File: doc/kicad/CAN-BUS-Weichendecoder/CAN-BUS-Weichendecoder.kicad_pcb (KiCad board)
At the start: 2 copper layers, 158.8 x 124.5 mm, 53 parts, among them J1 250-1404, J1001 Conn_01x02_Female, J1003 Conn_01x07_Female, J11 250-1406, J12 Wago 250-1406, J13 Wago 250-1406, J14 Wago 250-1406, J15 Wago 250-1406, J2 250-1404, J22 J22, J23 J22, J3 250-1404, J31 12V DC, J4 250-1404, J41 2604-1102, J5 250-1404, U1 Arduino_Nano, U10 TSR_1-2450, U1001 6N136, U2 ULN2803A, U3 ULN2803A, U4 PCF8574, U5 PCF8574, U6 PCF8574, U7 ULN2803A, U8 ULN2803A, U9 ULN2803A

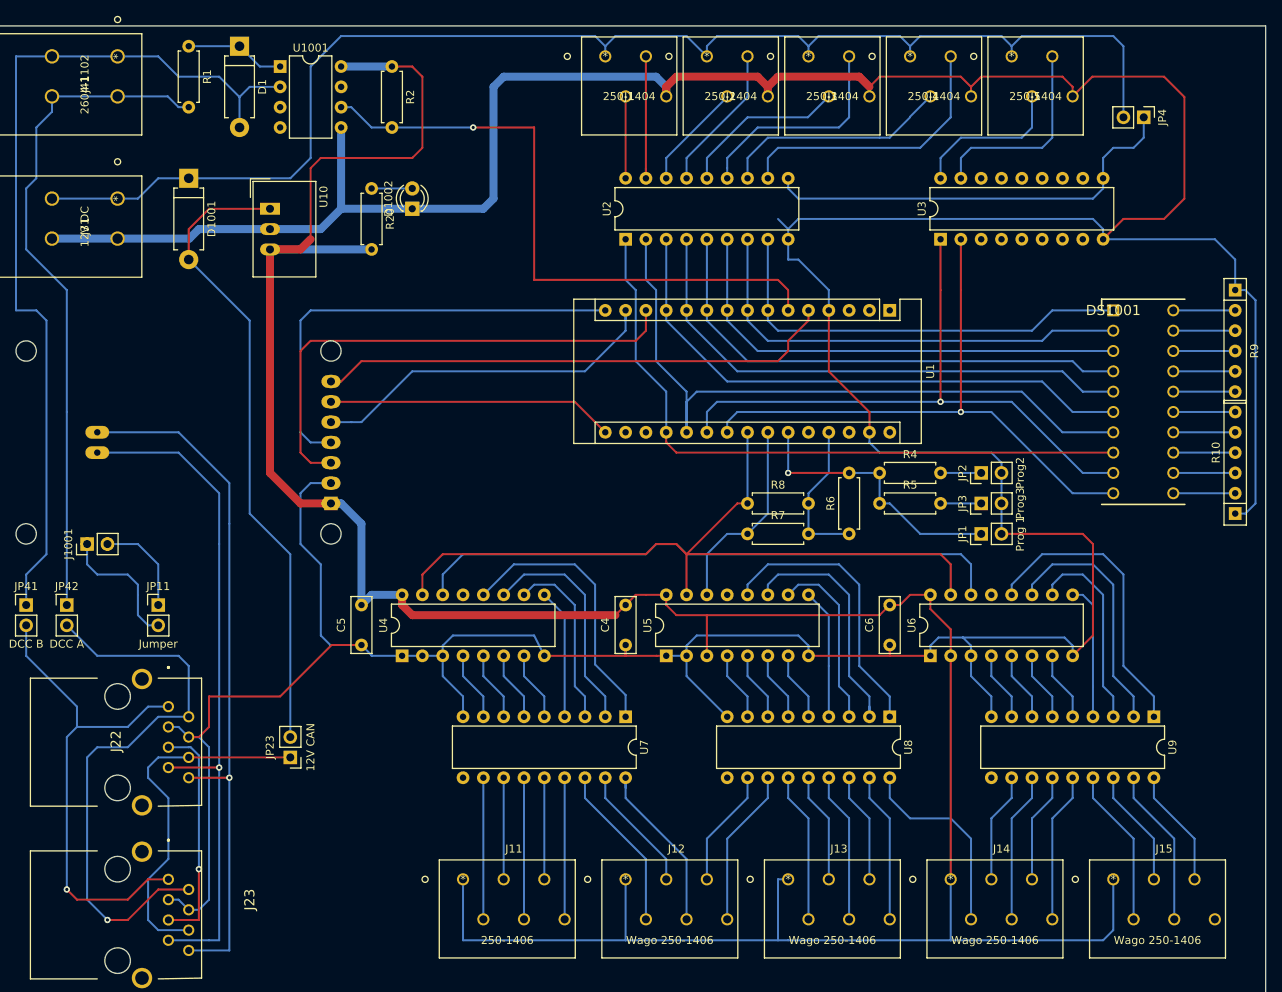
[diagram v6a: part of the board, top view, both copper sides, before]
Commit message: +5 analog zu GND verlegt
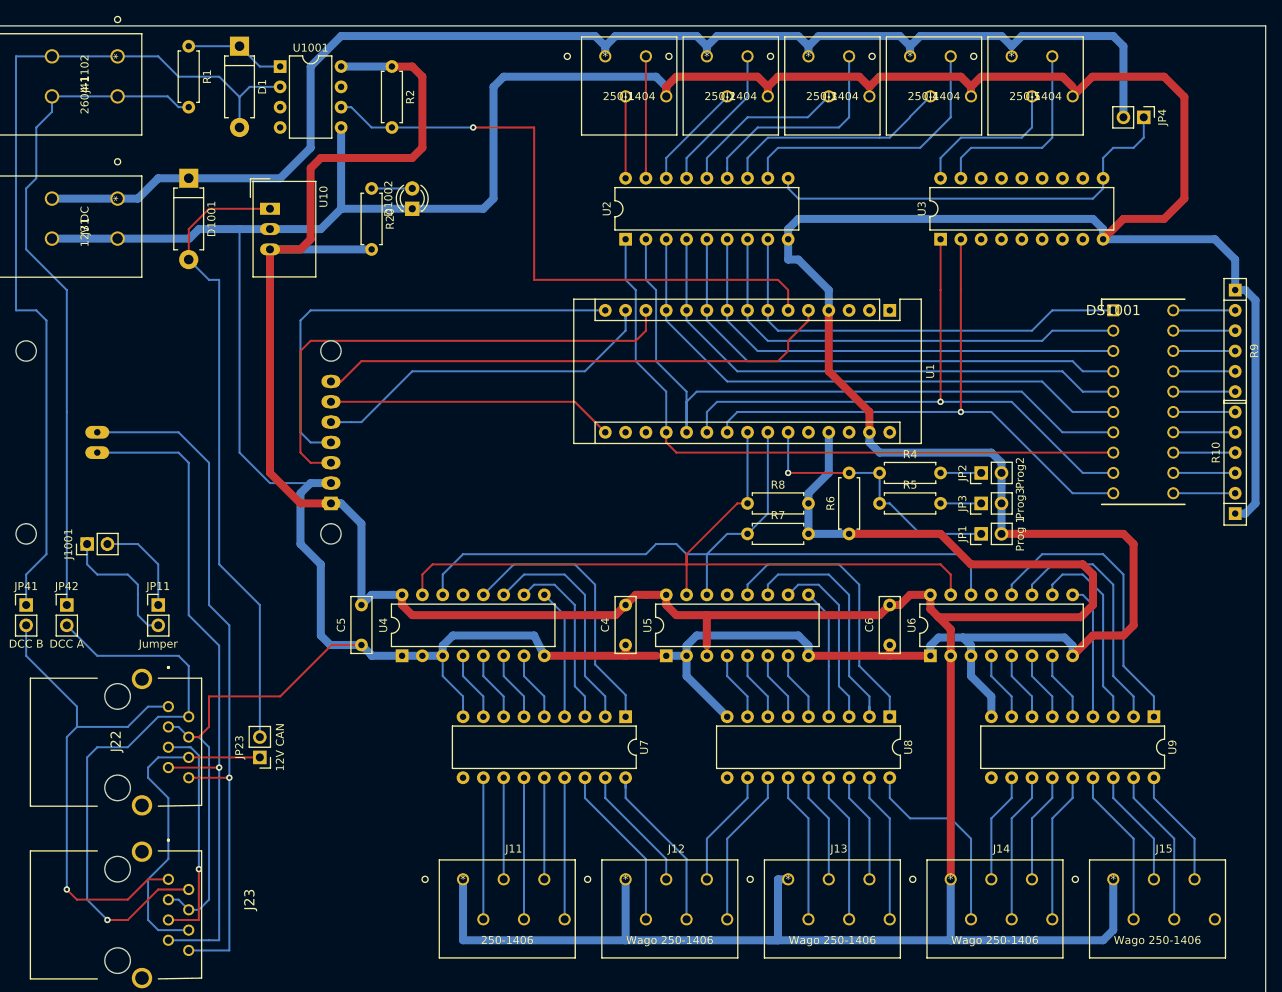
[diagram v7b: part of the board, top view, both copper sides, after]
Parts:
- moved JP23 3.81 mm to (86.4, 143.5)
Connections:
- Shield1001 pad 1: (no net) -> +5V
- Shield1001 pad 2: (no net) -> GND
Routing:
- net +5V: track 372.1 -> 429.7 mm
- net GND: track 611.2 -> 657.2 mm
- net Net-(J22-Pad6): track 45.1 -> 41.3 mm
- net Net-(R8-Pad1): track 99.2 -> 97.7 mm
- net +12V: track 170.6 -> 169.3 mm
- net Net-(D1001-Pad2): track 80.0 -> 79.1 mm

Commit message: verbessert
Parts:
- removed J1001: Conn_01x02_Female, Pin_Headers:Pin_Header_Straight_1x02_Pitch2.54mm
- removed J1003: Conn_01x07_Female, Pin_Headers:Pin_Header_Straight_1x07_Pitch2.54mm
- added H1: MountingHole, Mounting_Holes:MountingHole_3.2mm_M3, F.Cu at (207.0, 57.1)
- added H2: MountingHole, Mounting_Holes:MountingHole_3.2mm_M3, F.Cu at (205.7, 143.5)
- added H3: MountingHole, Mounting_Holes:MountingHole_3.2mm_M3, F.Cu at (114.3, 105.4)
- added H4: MountingHole, Mounting_Holes:MountingHole_3.2mm_M3, F.Cu at (101.6, 163.8)
- moved D1 10.2 mm to (94.0, 54.6)
- moved U10 10.2 mm to (97.8, 74.9)
- moved D1001 10.2 mm to (87.6, 71.1)
- moved D1002 10.2 mm to (115.6, 74.9)
- moved J31 10.2 mm to (78.7, 73.7)
- moved J41 10.2 mm to (78.7, 55.9)
- moved R1 10.2 mm to (87.6, 54.6)
- moved R2 10.2 mm to (113.0, 57.1)
- moved R20 10.2 mm to (110.5, 72.4)
- moved U1001 10.2 mm to (99.1, 57.1)
- moved JP41 8.89 mm to (66.0, 124.5)
- moved JP42 8.89 mm to (71.1, 124.5)
- moved Shield1001 8.89 mm to (106.7, 118.1)
- moved JP11 8.03 mm to (81.3, 127.0), turned to 180 degrees
- moved JP23 7.62 mm to (94.0, 143.5)
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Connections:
- JP11 pad 1: Net-(J1001-Pad2) -> Net-(JP11-Pad1)
- JP11 pad 2: Net-(J1001-Pad1) -> Net-(JP11-Pad2)
- Shield1001 pad 1.1: (no net) -> Net-(JP11-Pad1)
- Shield1001 pad 1.2: (no net) -> Net-(JP11-Pad2)
- Shield1001 pad 3: (no net) -> Net-(Shield1001-Pad3)
- Shield1001 pad 4: (no net) -> Net-(Shield1001-Pad4)
- Shield1001 pad 5: (no net) -> Net-(Shield1001-Pad5)
- Shield1001 pad 6: (no net) -> Net-(Shield1001-Pad6)
- Shield1001 pad 7: (no net) -> Net-(Shield1001-Pad7)
- U1 pad 13: Net-(J1003-Pad3) -> Net-(Shield1001-Pad3)
- U1 pad 14: Net-(J1003-Pad5) -> Net-(Shield1001-Pad5)
- U1 pad 15: Net-(J1003-Pad4) -> Net-(Shield1001-Pad4)
- U1 pad 16: Net-(J1003-Pad6) -> Net-(Shield1001-Pad6)
- U1 pad 5: Net-(J1003-Pad7) -> Net-(Shield1001-Pad7)
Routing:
- net Net-(J1003-Pad7): track 64.9 -> 0.00 mm
- net Net-(J1003-Pad3): track 63.8 -> 0.00 mm
- net Net-(Shield1001-Pad3): track 0.00 -> 57.8 mm
- net Net-(J1003-Pad4): track 56.9 -> 0.00 mm
- net Net-(Shield1001-Pad7): track 0.00 -> 55.2 mm
- net Net-(Shield1001-Pad4): track 0.00 -> 48.0 mm
- net Net-(J1003-Pad5): track 45.4 -> 0.00 mm
- net Net-(Shield1001-Pad5): track 0.00 -> 38.7 mm
- net Net-(J1003-Pad6): track 35.9 -> 0.00 mm
- net GND: track 657.2 -> 626.0 mm
- net Net-(Shield1001-Pad6): track 0.00 -> 28.2 mm
- net Net-(J1001-Pad1): track 16.8 -> 0.00 mm
- net Net-(JP11-Pad1): track 0.00 -> 14.1 mm
- net Net-(J1001-Pad2): track 12.5 -> 0.00 mm
- net Net-(JP11-Pad2): track 0.00 -> 11.2 mm
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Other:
- board size 158.8 x 124.5 mm -> 151.1 x 124.5 mm
